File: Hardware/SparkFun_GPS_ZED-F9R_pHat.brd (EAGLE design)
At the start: 65 x 57.3 mm, 120 parts, among them J1 QWIIC_RIGHT_ANGLE, J2 RASPBERRYPI-40-PIN-GPIO_SMD_S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, J4 U.FL, U1 UBLOX_ZED_F9R, U2 HCPL-270L

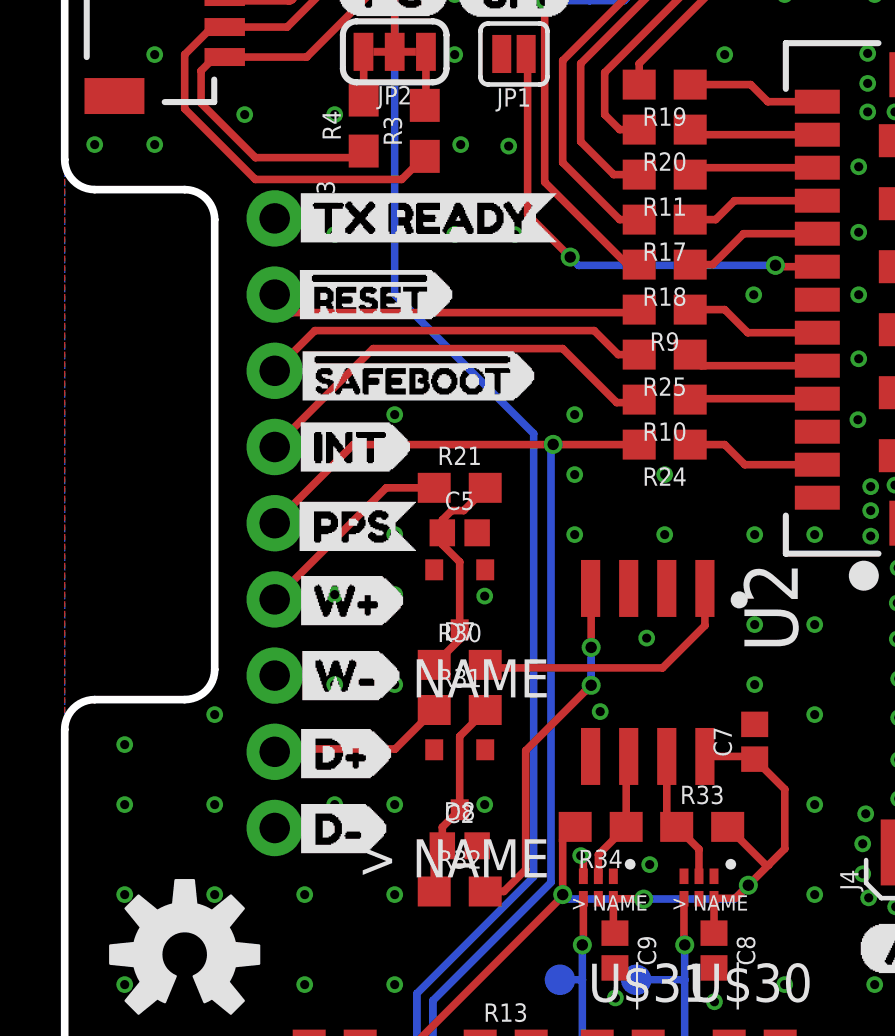
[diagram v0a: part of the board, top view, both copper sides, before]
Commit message: Replaces 9-pin connector with 8-pin
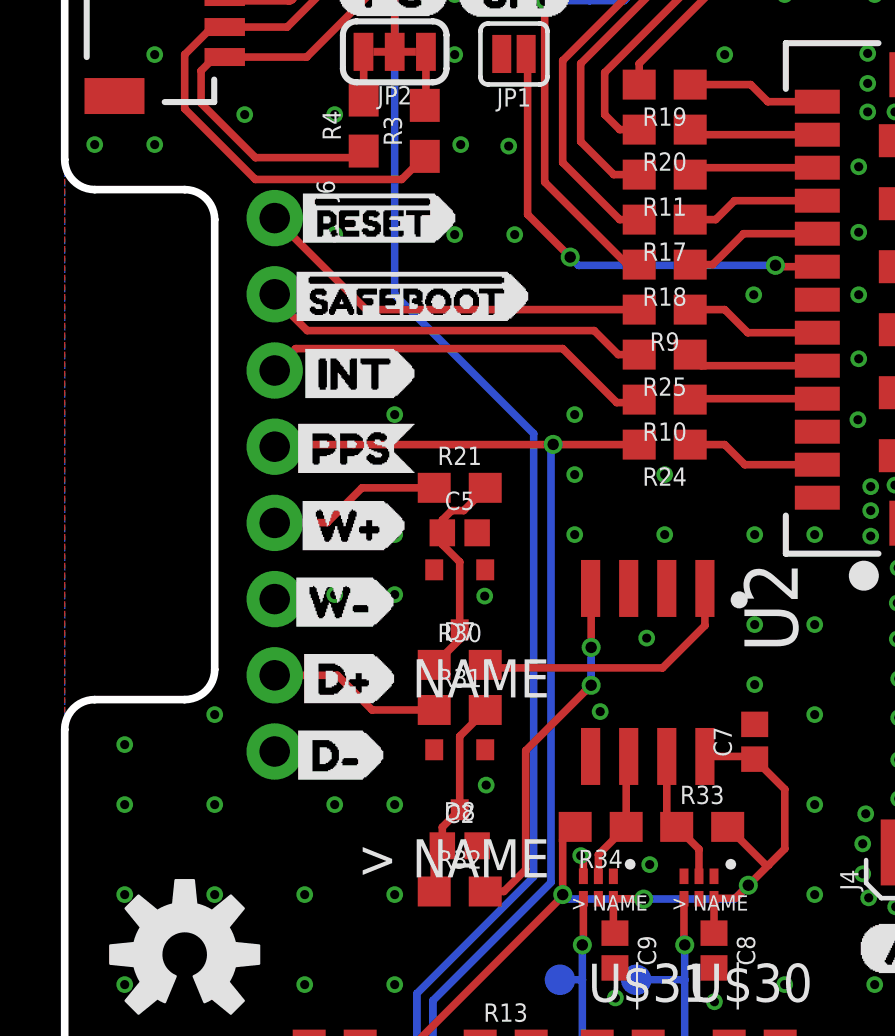
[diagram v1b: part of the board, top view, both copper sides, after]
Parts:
- removed J3: (no value), SparkFun-Connectors:1X09_NO_SILK
- removed U$17: (no value), bottom labels:TX_READY0
- removed U$9: (no value), ALL_LABELS:TX_READY0
- added J6: (no value), SparkFun-Connectors:1X08_NO_SILK
- moved U$15 2.66 mm to (15.8, 32.9)
- moved U$13 2.66 mm to (7.05, 32.9)
- moved U$12 2.60 mm to (11.7, 27.9)
- moved U$2 2.60 mm to (7.30, 27.9)
- moved U$7 2.55 mm to (7.30, 35.5)
- moved U$8 2.55 mm to (13.2, 35.5)
- moved U$22 2.50 mm to (7.50, 20.2)
- moved U$33 2.50 mm to (10.9, 20.2)
- moved U$34 2.50 mm to (11.4, 25.3)
- moved U$27 2.50 mm to (7.45, 25.3)
- moved U$28 2.46 mm to (7.20, 22.8)
- moved U$1 2.45 mm to (7.50, 30.4)
- moved U$32 2.45 mm to (10.8, 17.6)
- moved U$11 2.45 mm to (11.8, 30.4)
- moved U$23 2.45 mm to (7.30, 17.6)
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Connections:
- net !RESET: now also J6.1; no longer J3.2
- net !SAFEBOOT: now also J6.2; no longer J3.3
- net DIR+: now also J6.7; no longer J3.8
- net GND: now also J6.6, J6.8; no longer J3.7, J3.9
- net INT: now also J6.3; no longer J3.4
- net PPS: now also J6.4; no longer J3.5
- net WT+: now also J6.5; no longer J3.6
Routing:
- net WT+: track 6.86 -> 5.80 mm
- net INT: track 14.3 -> 13.3 mm
- net !RESET: track 12.4 -> 13.4 mm
- net PPS: track 39.5 -> 38.6 mm
- net GND: vias 304 -> 302

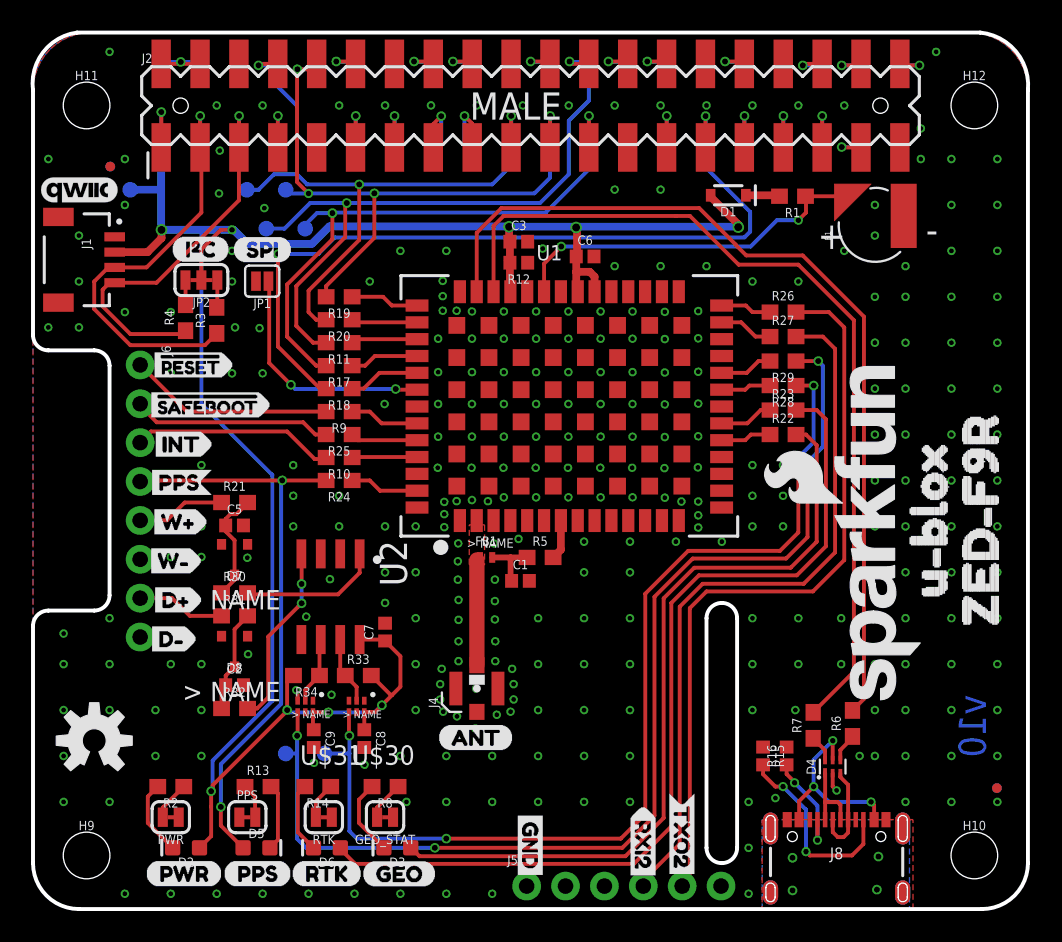
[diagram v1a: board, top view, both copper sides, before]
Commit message: Renumbers parts, adds PROD_ID for new parts
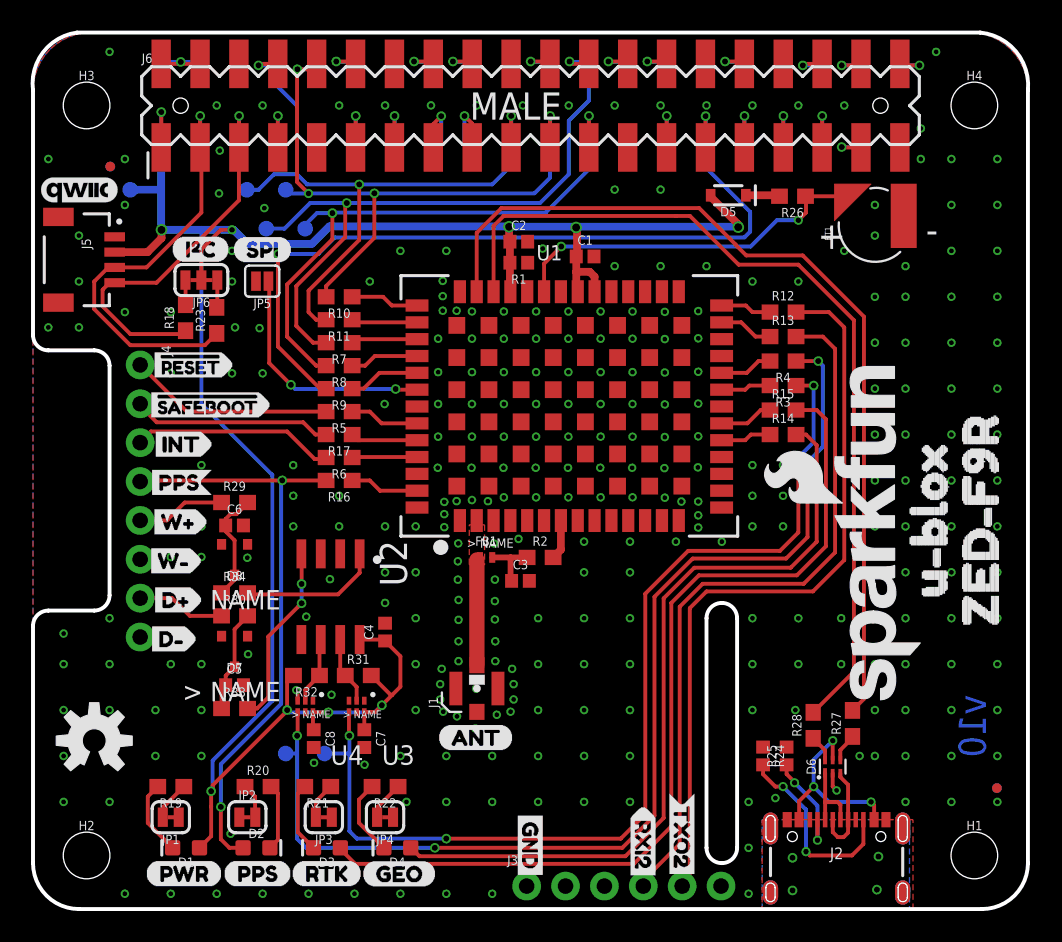
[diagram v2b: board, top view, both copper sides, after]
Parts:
- removed C9: 0.1uF, SparkFun-Capacitors:0402
- removed FD10, FD11, FD12, FD9: FIDUCIALUFIDUCIAL, SparkFun-Aesthetics:FIDUCIAL-MICRO
- removed J8: (no value), SparkFun-Connectors:USB-C-16P
- removed PPS, PWR: JUMPER-SMT_2_NC_TRACE_SILK, SparkFun-Jumpers:SMT-JUMPER_2_NC_TRACE_SILK
- added C4: 0.1uF, SparkFun-Capacitors:0402
- added FD1, FD2, FD3, FD4: FIDUCIALUFIDUCIAL, SparkFun-Aesthetics:FIDUCIAL-MICRO
- added J3: (no value), SparkFun-Connectors:1X06_NO_SILK
- added JP5: JUMPER-SMT_2_NO_SILK, SparkFun-Jumpers:SMT-JUMPER_2_NO_SILK
- added JP6: JUMPER-SMT_3_2-NC_TRACE_SILK, SparkFun-Jumpers:SMT-JUMPER_3_2-NC_TRACE_SILK
- C1: value 47pF -> 1.0uF
- C2: value 1nF -> 1.0uF
- C3: value 1.0uF -> 47pF
- C6: value 1.0uF -> 1nF
- D1: value 0.5A/40V/420mV -> RED; device SparkFun-DiscreteSemi:SOD-323 -> SparkFun-LED:LED-0603
- D2: value RED -> BLUE
- D4: value PRTR5V0U2F -> BLUE; device SparkFun-IC-Power:SOT886 -> SparkFun-LED:LED-0603
- D5: value BLUE -> 0.5A/40V/420mV; device SparkFun-LED:LED-0603 -> SparkFun-DiscreteSemi:SOD-323
- D6: value BLUE -> PRTR5V0U2F; device SparkFun-LED:LED-0603 -> SparkFun-IC-Power:SOT886
- J1: value QWIIC_RIGHT_ANGLE -> U.FL; device SparkFun-Connectors:JST04_1MM_RA -> SparkFun-Connectors:U.FL
- J2: value RASPBERRYPI-40-PIN-GPIO_SMD_STACK_NOHOLES_NOREF -> (none); device SparkFun-Connectors:RASPBERRY_PI_HAT_40_PIN_SMD_STACKABLE_NOHOLES_NOREF -> SparkFun-Connectors:USB-C-16P
- J4: value U.FL -> (none); device SparkFun-Connectors:U.FL -> SparkFun-Connectors:1X08_NO_SILK
- J5: value (none) -> QWIIC_RIGHT_ANGLE; device SparkFun-Connectors:1X06_NO_SILK -> SparkFun-Connectors:JST04_1MM_RA
- J6: value (none) -> RASPBERRYPI-40-PIN-GPIO_SMD_STACK_NOHOLES_NOREF; device SparkFun-Connectors:1X08_NO_SILK -> SparkFun-Connectors:RASPBERRY_PI_HAT_40_PIN_SMD_STACKABLE_NOHOLES_NOREF
- JP1: value JUMPER-SMT_2_NO_SILK -> JUMPER-SMT_2_NC_TRACE_SILK; device SparkFun-Jumpers:SMT-JUMPER_2_NO_SILK -> SparkFun-Jumpers:SMT-JUMPER_2_NC_TRACE_SILK
- JP2: value JUMPER-SMT_3_2-NC_TRACE_SILK -> JUMPER-SMT_2_NC_TRACE_SILK; device SparkFun-Jumpers:SMT-JUMPER_3_2-NC_TRACE_SILK -> SparkFun-Jumpers:SMT-JUMPER_2_NC_TRACE_SILK
- LOGO1: value SFE_LOGO_NAME_FLAME.2_INCH -> QWIIC_LOGO_5MM; device SparkFun-Aesthetics:SFE_LOGO_NAME_FLAME_.2 -> SparkFun-Aesthetics:QWIIC_5MM
- LOGO3: value QWIIC_LOGO_5MM -> SFE_LOGO_NAME_FLAME.2_INCH; device SparkFun-Aesthetics:QWIIC_5MM -> SparkFun-Aesthetics:SFE_LOGO_NAME_FLAME_.2
- R1: value 3.3k -> 100K; device SparkFun-Resistors:0603 -> SparkFun-Resistors:0402
- R12: value 100K -> 33; device SparkFun-Resistors:0402 -> SparkFun-Resistors:0603
- R13, R14, R2, R8: value 1k -> 33
- R15, R16: value 5.1k -> 33; device SparkFun-Resistors:0402 -> SparkFun-Resistors:0603
- R18, R23: value 33 -> 2.2k
- R19, R20, R22: value 33 -> 1k
- R21: value 3.3k -> 1k
- R24, R25: value 33 -> 5.1k; device SparkFun-Resistors:0603 -> SparkFun-Resistors:0402
- R26, R29: value 33 -> 3.3k
- R27, R28: value 33 -> 27
- R3, R4: value 2.2k -> 33
- R30: value 470 -> 3.3k
- R31: value 3.3k -> 910; device SparkFun-Resistors:0603 -> classified:0603
- R32: value 470 -> 910; device SparkFun-Resistors:0603 -> classified:0603
- R33, R34: value 910 -> 470; device classified:0603 -> SparkFun-Resistors:0603
- R6, R7: value 27 -> 33
- U2: value HCPL-270L -> HCPL-073L
- moved J2 63.1 mm to (52.5, 6.18)
- moved LOGO1 56.7 mm to (3.00, 47.0), turned to 0 degrees
- moved LOGO3 56.7 mm to (55.1, 24.6), turned to 90 degrees
- moved D1 55.4 mm to (10.0, 4.00)
- moved D5 52.6 mm to (45.4, 46.6), turned to 180 degrees
- moved J5 49.0 mm to (5.33, 42.4), turned to 270 degrees
- moved R13 45.2 mm to (49.0, 37.4)
- moved R7 39.8 mm to (20.0, 37.0), turned to 180 degrees
- moved R4 39.1 mm to (49.0, 35.8), turned to 180 degrees
- moved R14 38.1 mm to (49.0, 31.0), turned to 0 degrees
- moved R6 37.8 mm to (20.0, 29.5), turned to 180 degrees
- moved R23 37.5 mm to (12.0, 38.5), turned to 90 degrees
- moved R3 37.2 mm to (49.0, 34.2), turned to 180 degrees
- moved R29 37.0 mm to (13.2, 26.6), turned to 0 degrees
- moved J1 36.7 mm to (29.0, 14.4), turned to 90 degrees
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- renumbered B1 to BT1, FRAME2 to FRAME1, GEO_STAT to JP4, H10 to H1, H11 to H3, H12 to H4, H9 to H2, RTK to JP3, U$30 to U3, U$31 to U4
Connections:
- net !RESET: now also J4.1, R5.2; no longer J6.1, R9.2
- net !SAFEBOOT: now also J4.2, R17.2; no longer J6.2, R25.2
- net 3.3V: now also C1.1, C2.1, C4.1, D5.A, J5.2, J6.1, J6.17, J6.17B, J6.1B, JP6.2, R1.2, R31.2, R32.2; no longer C3.1, C6.1, C9.1, D2.A, J1.2, J2.1, J2.17, J2.17B, J2.1B, JP2.2, R12.2, R33.2, R34.2
- net 5V: now also J6.2, J6.2B, J6.4, J6.4B; no longer J2.2, J2.2B, J2.4, J2.4B
- net CE1: now also J6.26, J6.26B; no longer J2.26, J2.26B
- net DIR+: now also J4.7, R30.1; no longer J6.7, R31.1
- net DIR_IN: now also R33.2; no longer R32.2
- net DIR_OUT: now also R4.1; no longer R29.1
- net DIR_SCHMITT: now also R32.1; no longer R34.1
- net DMINUS: now also R28.2; no longer R7.2
- net DPLUS: now also R27.2; no longer R6.2
- net D_SEL: now also JP5.1; no longer JP1.1
- net GEOF_STAT: now also D4.A, R14.2; no longer D3.A, R22.2
- net GND: now also C4.2, D6.2, J1.2, J2.GND, J2.GND2, J3.1, J4.6, J4.8, J6.14, J6.14B, J6.20, J6.20B, J6.25, J6.25B, J6.30, J6.30B, J6.34, J6.34B, J6.39, J6.39B, J6.6B, J6.9, J6.9B, JP1.1, JP2.1, JP5.2, R1.1, R24.1, R25.1; no longer C9.2, D4.2, J2.14, J2.14B, J2.20, J2.20B, J2.25, J2.25B, J2.30, J2.30B, J2.34, J2.34B, J2.39, J2.39B, J2.6, J2.6B, J2.9, J2.9B, J4.1, J4.2, J6.8, J8.GND, J8.GND2, JP1.2, PPS.1, PWR.1, R12.1, R15.1, R16.1
- net GP12: now also J6.32, J6.32B; no longer J2.32, J2.32B
- net GP13: now also J6.33, J6.33B; no longer J2.33, J2.33B
- net GP16: now also J6.36, J6.36B; no longer J2.36, J2.36B
- net GP17: now also J6.11, J6.11B; no longer J2.11, J2.11B
- net GP18: now also J6.12, J6.12B; no longer J2.12, J2.12B
- net GP19: now also J6.35, J6.35B; no longer J2.35, J2.35B
- net GP20: now also J6.38, J6.38B; no longer J2.38, J2.38B
- net GP21: now also J6.40, J6.40B; no longer J2.40, J2.40B
- net GP22: now also J6.15, J6.15B; no longer J2.15, J2.15B
- net GP23: now also J6.16, J6.16B; no longer J2.16, J2.16B
- net GP24: now also J6.18, J6.18B; no longer J2.18, J2.18B
- net GP25: now also J6.22, J6.22B; no longer J2.22, J2.22B
- net GP26: now also J6.37, J6.37B; no longer J2.37, J2.37B
- net GP27: now also J6.13, J6.13B; no longer J2.13, J2.13B
- net GP4: now also J6.7, J6.7B; no longer J2.7, J2.7B
- net GP6: now also J6.31, J6.31B; no longer J2.31, J2.31B
- net ID_SC: now also J6.28, J6.28B; no longer J2.28, J2.28B
- net ID_SD: now also J6.27, J6.27B; no longer J2.27, J2.27B
- net INT: now also J4.3, R6.2; no longer J6.3, R10.2
- net N$1: now also JP6.1, R23.2; no longer JP2.1, R3.2
- net N$10: now also D6.5, J2.VBUS1, J2.VBUS2; no longer D4.5, J8.VBUS1, J8.VBUS2
- net N$11: now also D6.1, J2.A7, J2.B7; no longer D4.1, J8.A7, J8.B7
- net N$12: now also J2.B5, R24.2; no longer J8.B5, R15.2
- net N$13: now also R5.1; no longer R9.1
- net N$14: now also R6.1; no longer R10.1
- net N$15: now also R7.1; no longer R11.1
- net N$16: now also R22.1; no longer R8.1
- net N$17: now also D4.C, R22.2; no longer D3.C, R8.2
- net N$18: now also J2.A5, R25.2; no longer J8.A5, R16.2
- net N$19: now also R8.1; no longer R17.1
- net N$2: now also D5.C, R26.2; no longer D1.C, R1.2
- net N$20: now also R9.1; no longer R18.1
- net N$21: now also R10.1; no longer R19.1
- net N$22: now also R21.1; no longer R14.1
- net N$23: now also JP2.2, R20.1; no longer PPS.2, R13.1
- net N$24: now also D2.C, R20.2; no longer D5.C, R13.2
- net N$25: now also D3.C, R21.2; no longer D6.C, R14.2
- net N$26: now also R11.1; no longer R20.1
- net N$27: now also C6.1, D8.P3, R29.2, R34.1; no longer C5.1, D7.P3, R21.2, R30.1
- net N$28: now also R14.1; no longer R22.1
- net N$29: now also R15.1; no longer R23.1
- net N$3: now also JP6.3, R18.2; no longer JP2.3, R4.2
- net N$30: now also R16.1; no longer R24.1
- net N$31: now also R17.1; no longer R25.1
- net N$32: now also R12.1; no longer R26.1
- net N$33: now also R13.1; no longer R27.1
- net N$34: now also R3.2; no longer R28.2
- net N$35: now also R4.2; no longer R29.2
- net N$36: now also C5.1, D7.P3, R30.2, R33.1; no longer C2.1, D8.P3, R31.2, R32.1
- net N$4: now also D1.C, R19.2; no longer D2.C, R2.2
- net N$5: now also C3.1, R2.1; no longer C1.1, R5.1
- net N$6: now also D6.6, R28.1; no longer D4.6, R7.1
- net N$7: now also D6.4, R27.1; no longer D4.4, R6.1
- net N$8: now also JP1.2, R19.1; no longer PWR.2, R2.1
- net N$9: now also D6.3, J2.A6, J2.B6; no longer D4.3, J8.A6, J8.B6
- net PPS: now also D2.A, J4.4, R16.2; no longer D5.A, J6.4, R24.2
- net QWIIC_SCL: now also J5.4, J6.5, J6.5B, R18.1; no longer J1.4, J2.5, J2.5B, R4.1
- net QWIIC_SDA: now also J5.3, J6.3, J6.3B, R23.1; no longer J1.3, J2.3, J2.3B, R3.1
- net RF_IN: now also J1.FEED; no longer J4.FEED
- net RTK_STAT: now also D3.A, R15.2; no longer D6.A, R23.2
- net RXI/MOSI: now also J6.19, J6.19B, J6.8, J6.8B, R11.2; no longer J2.19, J2.19B, J2.8, J2.8B, R20.2
- net RXI2: now also J3.4, R13.2; no longer J5.4, R27.2
- net SCL/CLK: now also J6.23, J6.23B, R8.2; no longer J2.23, J2.23B, R17.2
- net SDA/!CS: now also J6.24, J6.24B, R7.2; no longer J2.24, J2.24B, R11.2
- net SHIELD: now also J2.SHLD1, J2.SHLD2, J2.SHLD3, J2.SHLD4, J2.SHLD5, J2.SHLD6, J2.SHLD7, J2.SHLD8; no longer J8.SHLD1, J8.SHLD2, J8.SHLD3, J8.SHLD4, J8.SHLD5, J8.SHLD6, J8.SHLD7, J8.SHLD8
- net TXO/MISO: now also J6.10, J6.10B, J6.21, J6.21B, R10.2; no longer J2.10, J2.10B, J2.21, J2.21B, R19.2
- net TXO2: now also J3.5, R12.2; no longer J5.5, R26.2
- net TX_READY: now also J6.29, J6.29B, R9.2; no longer J2.29, J2.29B, R18.2
- net V_BATT: now also R26.1; no longer R1.1
- net V_RF: now also R2.2; no longer R5.2
- net WT+: now also J4.5, R29.1; no longer J6.5, R21.1
- net WT_IN: now also R34.2; no longer R30.2
- net WT_OUT: now also R3.1; no longer R28.1
- net WT_SCHMITT: now also R31.1; no longer R33.1
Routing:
- net GND: track 2.13 -> 1.96 mm, vias 302 -> 303

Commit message: Fixe RF trace, fixes silk, moves version number, fixes D+ and D- traces
* Changes jumper labels in schematic
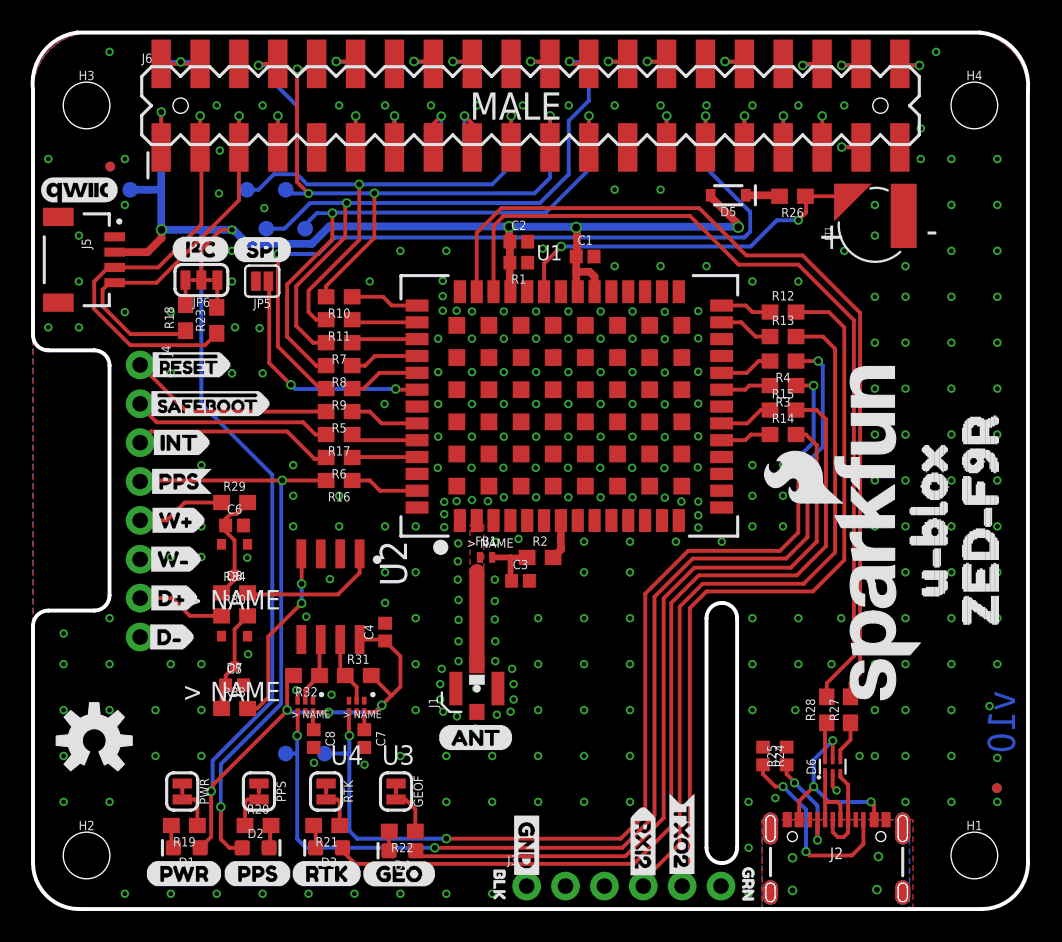
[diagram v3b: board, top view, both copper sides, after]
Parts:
- removed JP1, JP2, JP3, JP4: JUMPER-SMT_2_NC_TRACE_SILK, SparkFun-Jumpers:SMT-JUMPER_2_NC_TRACE_SILK
- added GEOF, PPS, PWR, RTK: JUMPER-SMT_2_NC_TRACE_SILK, SparkFun-Jumpers:SMT-JUMPER_2_NC_TRACE_SILK
- added U$17: (no value), TXR:BLK2
- added U$30: (no value), TXR:GRN1
- added U$9: (no value), SparkFun-Aesthetics:SFE_LOGO_NAME_FLAME_.3
- moved R22 3.13 mm to (24.1, 5.08)
- moved R19 2.69 mm to (9.89, 5.46)
- moved R21 2.61 mm to (19.2, 5.46)
- moved R20 2.54 mm to (14.7, 5.46)
- moved R28 1.35 mm to (51.9, 13.0)
- moved R27 0.90 mm to (53.4, 13.0)
- moved D4 0.38 mm to (24.1, 3.81)
- moved U$22 0.28 mm to (7.25, 20.3)
- moved U$33 0.28 mm to (10.6, 20.3)
- moved U$18 0.24 mm to (32.2, 6.59)
- moved U$19 0.24 mm to (32.2, 1.76)
- moved U$23 0.18 mm to (7.17, 17.8)
- moved U$1 0.17 mm to (7.37, 30.5)
- moved U$11 0.17 mm to (11.6, 30.5)
- moved U$34 0.16 mm to (11.3, 25.4)
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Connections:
- net GND: now also GEOF.1, PPS.1, PWR.1, RTK.1; no longer JP1.1, JP2.1, JP3.1, JP4.1
- net N$16: now also GEOF.2; no longer JP4.2
- net N$22: now also RTK.2; no longer JP3.2
- net N$23: now also PPS.2; no longer JP2.2
- net N$8: now also PWR.2; no longer JP1.2
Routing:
- net N$17: track 5.03 -> 1.28 mm
- net N$4: track 4.94 -> 1.51 mm
- net N$25: track 4.61 -> 1.51 mm
- net N$24: track 4.40 -> 1.51 mm
- net DMINUS: track 57.6 -> 56.3 mm
- net DPLUS: track 58.8 -> 57.7 mm
- net N$7: track 1.87 -> 2.71 mm
- net RF_IN: track 6.88 -> 6.12 mm
- net N$6: track 1.74 -> 2.48 mm
- net GND: vias 303 -> 301
